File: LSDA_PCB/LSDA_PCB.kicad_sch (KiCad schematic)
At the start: 37 parts, among them Q1 BC547, Q2 BC547, U1 LM324

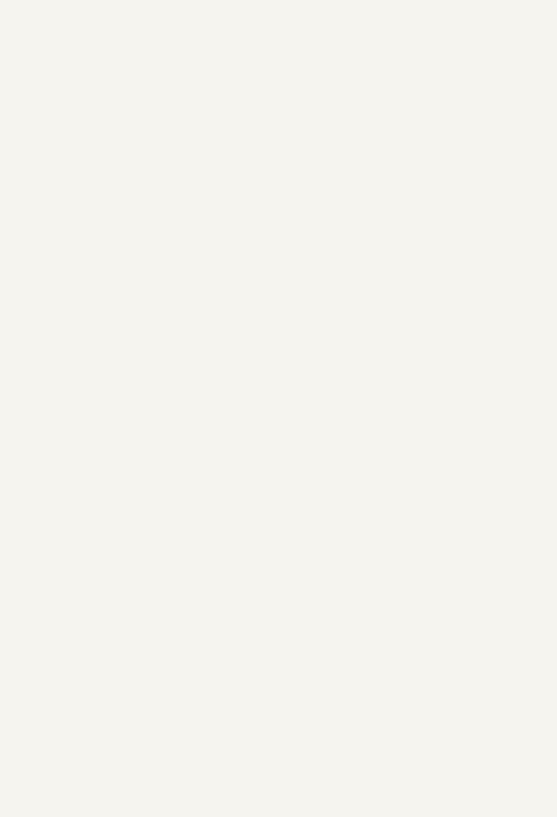
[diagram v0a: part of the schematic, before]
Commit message: Mounting holes
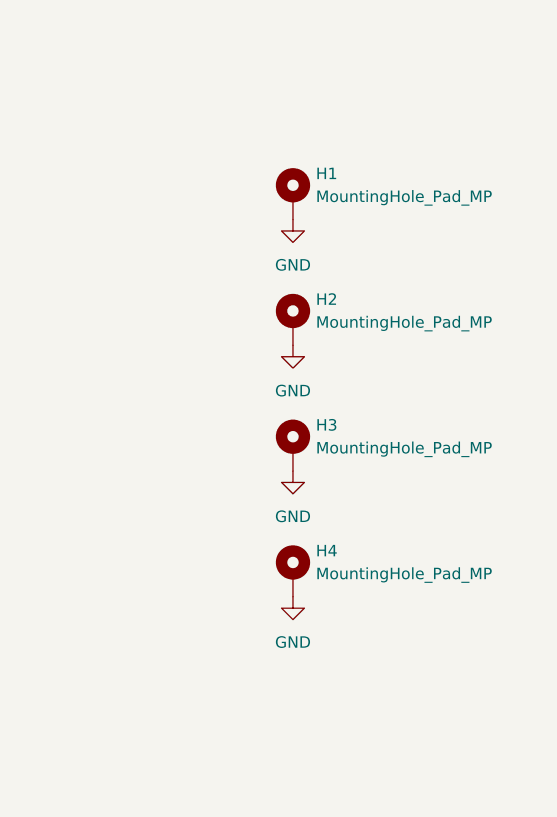
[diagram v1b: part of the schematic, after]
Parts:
- added H1, H2, H3, H4: MountingHole_Pad_MP, MountingHole:MountingHole_3.2mm_M3_ISO7380_Pad, symbol Mechanical:MountingHole_Pad_MP
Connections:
- net GND: now also H1.MP, H2.MP, H3.MP, H4.MP
